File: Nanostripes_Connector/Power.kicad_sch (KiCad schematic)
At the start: 5 parts, among them U1 78L03

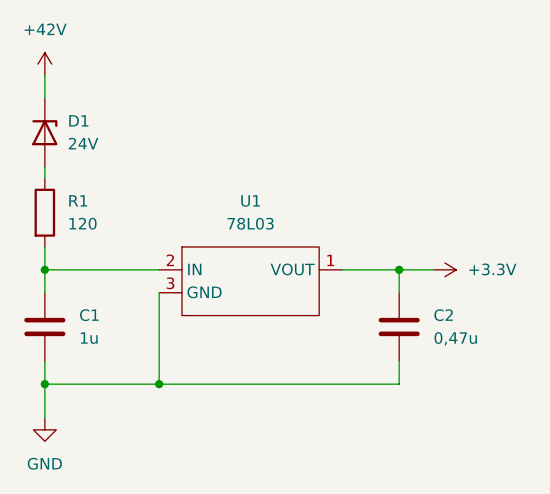
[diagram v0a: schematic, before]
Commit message: updated component values
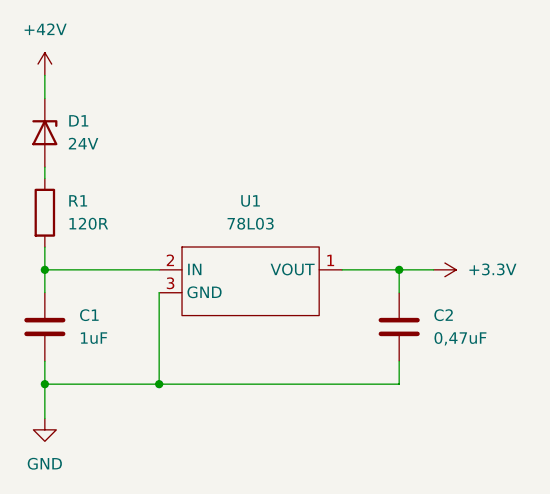
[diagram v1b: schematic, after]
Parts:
- C1: value 1u -> 1uF
- C2: value 0,47u -> 0,47uF
- R1: value 120 -> 120R
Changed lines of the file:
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@@
 			)
 		)
-		(property "Value" "120"
+		(property "Value" "120R"
 			(at 27.94 39.3699 0)
 			(effects
@@
 			)
 		)
-		(property "Value" "0,47u"
+		(property "Value" "0,47uF"
 			(at 68.58 52.0699 0)
 			(effects
@@
 			)
 		)
-		(property "Value" "1u"
+		(property "Value" "1uF"
 			(at 29.21 52.0699 0)
 			(effects
